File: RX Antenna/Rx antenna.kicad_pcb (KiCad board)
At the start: 2 copper layers, 40 x 40 mm, 11 parts, among them J1 PATCH_FEED, J2 Conn_01x02

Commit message: pcb for rx made
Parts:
- removed D1: MA4E2054A1-287T, Package_TO_SOT_SMD:SOT-23
- removed J2: Conn_01x02, Connector_PinHeader_2.54mm:PinHeader_1x02_P2.54mm_Vertical
- removed JP1: SolderJumper_3_Bridged12, Jumper:SolderJumper-3_P1.3mm_Bridged12_RoundedPad1.0x1.5mm
- removed TP_DC1, TP_RF1, TP_STORE1: TestPoint, TestPoint:TestPoint_Pad_D1.5mm
- added AE1: Antenna, customFootprints:AperturePatch, F.Cu at (115.0, 115.0)
- added C4: 2p, Capacitor_SMD:C_0201_0603Metric_Pad0.64x0.40mm_HandSolder, B.Cu at (128.2, 118.8)
- added C5: 0.1u, Capacitor_SMD:C_0603_1608Metric_Pad1.08x0.95mm_HandSolder, B.Cu at (125.4, 110.0)
- added C6: 10u, Capacitor_SMD:C_0603_1608Metric_Pad1.08x0.95mm_HandSolder, B.Cu at (126.4, 111.1)
- added C7: 0.01u, Capacitor_SMD:C_0603_1608Metric_Pad1.08x0.95mm_HandSolder, B.Cu at (124.5, 117.8)
- added C8: 0.76pF, customFootprints:C_0201_branch, B.Cu at (121.0, 124.1)
- added CR1: SMS7630-006LF, Package_TO_SOT_SMD:SOT-23, B.Cu at (126.0, 119.8)
- added D2: LED, LED_SMD:LED_0603_1608Metric_Pad1.05x0.95mm_HandSolder, B.Cu at (121.8, 105.2)
- added D3: LED, LED_SMD:LED_0603_1608Metric_Pad1.05x0.95mm_HandSolder, B.Cu at (120.7, 106.3)
- added L2: 22u, Inductor_SMD:L_1210_3225Metric_Pad1.42x2.65mm_HandSolder, B.Cu at (128.3, 114.3)
- added Q1: AO3400A, Package_TO_SOT_SMD:SOT-23, B.Cu at (123.5, 108.4)
- added R1: 10M, Resistor_SMD:R_0603_1608Metric_Pad0.98x0.95mm_HandSolder, B.Cu at (121.6, 117.7)
- added R10: 0, Resistor_SMD:R_0603_1608Metric_Pad0.98x0.95mm_HandSolder, B.Cu at (118.0, 107.4)
- added R11: 0, Resistor_SMD:R_0603_1608Metric_Pad0.98x0.95mm_HandSolder, B.Cu at (119.4, 102.8)
- added R12: 0, Resistor_SMD:R_0603_1608Metric_Pad0.98x0.95mm_HandSolder, B.Cu at (118.3, 103.9)
- added R2: 4.42M, Resistor_SMD:R_0603_1608Metric_Pad0.98x0.95mm_HandSolder, B.Cu at (119.3, 120.0)
- added R3: 3.65M, Resistor_SMD:R_0603_1608Metric_Pad0.98x0.95mm_HandSolder, B.Cu at (120.5, 116.6)
- added R4: 4.42M, Resistor_SMD:R_0603_1608Metric_Pad0.98x0.95mm_HandSolder, B.Cu at (118.2, 118.9)
- added R5: 10M, Resistor_SMD:R_0603_1608Metric_Pad0.98x0.95mm_HandSolder, B.Cu at (129.3, 118.5)
- added R6: 10M, Resistor_SMD:R_0603_1608Metric_Pad0.98x0.95mm_HandSolder, B.Cu at (129.3, 121.9)
- added R7: 10M, Resistor_SMD:R_0603_1608Metric_Pad0.98x0.95mm_HandSolder, B.Cu at (119.3, 110.9)
- added R8: 0, Resistor_SMD:R_0603_1608Metric_Pad0.98x0.95mm_HandSolder, B.Cu at (116.9, 108.5)
- added R9: 10M, Resistor_SMD:R_0603_1608Metric_Pad0.98x0.95mm_HandSolder, B.Cu at (120.4, 109.8)
- added U1: BQ25504, Package_DFN_QFN:VQFN-16-1EP_3x3mm_P0.5mm_EP1.68x1.68mm, B.Cu at (123.8, 114.4)
- C1: value 2.2pF -> 0.76pF; footprint Capacitor_SMD:C_0402_1005Metric -> Capacitor_SMD:C_0201_0603Metric_Pad0.64x0.40mm_HandSolder; moved to B.Cu
- C2: value 10nF -> 2p; footprint Capacitor_SMD:C_0402_1005Metric -> Capacitor_SMD:C_0201_0603Metric_Pad0.64x0.40mm_HandSolder; moved to B.Cu
- C3: value 100mF 5.5V -> 3mF
- J1: value PATCH_FEED -> Conn_Coaxial; footprint Connector_PinHeader_2.54mm:PinHeader_1x01_P2.54mm_Vertical -> Connector_Coaxial:U.FL_Hirose_U.FL-R-SMT-1_Vertical; moved to B.Cu
- L1: value 1.8nH -> 2.51nH; moved to B.Cu
- moved J1 79.7 mm to (121.0, 128.0), turned to -90 degrees
- moved L1 73.6 mm to (122.0, 122.5), turned to 45 degrees
- moved C1 72.3 mm to (121.4, 123.7), turned to -45 degrees
- moved C2 68.7 mm to (123.3, 121.2), turned to 45 degrees
- moved C3 50.5 mm to (125.2, 105.6), turned to -45 degrees
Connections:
- C1 pad 1: Net-(D1-A) -> Net-(AE1-A)
- C2 pad 1: Net-(D1-K) -> Net-(C2-Pad1)
- C2 pad 2: GND -> Net-(C2-Pad2)
- C3 pad 1: Net-(D1-K) -> Net-(U1-VBAT)
- L1 pad 1: Net-(JP1-C) -> Net-(AE1-A)
- L1 pad 2: Net-(D1-A) -> Net-(C2-Pad1)
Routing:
- net GND: track 0.00 -> 19.5 mm, vias 0 -> 8
- net Net-(U1-VRDIV): track 0.00 -> 19.5 mm
- net Net-(U1-VBAT): track 0.00 -> 17.8 mm
- net Net-(U1-OK_HYST): track 0.00 -> 9.16 mm
- net Net-(U1-VOC_SAMP): track 0.00 -> 9.12 mm, vias 0 -> 2
- net Net-(U1-VIN_DC): track 0.00 -> 8.87 mm
- net Net-(U1-OK_PROG): track 0.00 -> 8.09 mm
- net Net-(AE1-A): track 0.00 -> 7.49 mm
- net Net-(Q1-G): track 0.00 -> 6.80 mm
- net Net-(U1-VBAT_OV): track 0.00 -> 5.95 mm
- net Net-(U1-VBAT_UV): track 0.00 -> 5.38 mm
- net Net-(U1-VSTOR): track 0.00 -> 3.69 mm
- net Net-(U1-LBST): track 0.00 -> 3.33 mm
- net Net-(D3-K): track 0.00 -> 2.77 mm
- net Net-(J1-In): track 0.07 -> 2.44 mm
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- added copper zone on B.Cu, net GND
- added copper zone on In2.Cu, net GND
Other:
- board size 40 x 40 mm -> 30 x 30 mm
- copper layers 2 -> 4
- rule pad_to_mask_clearance: 0 -> 0.0508

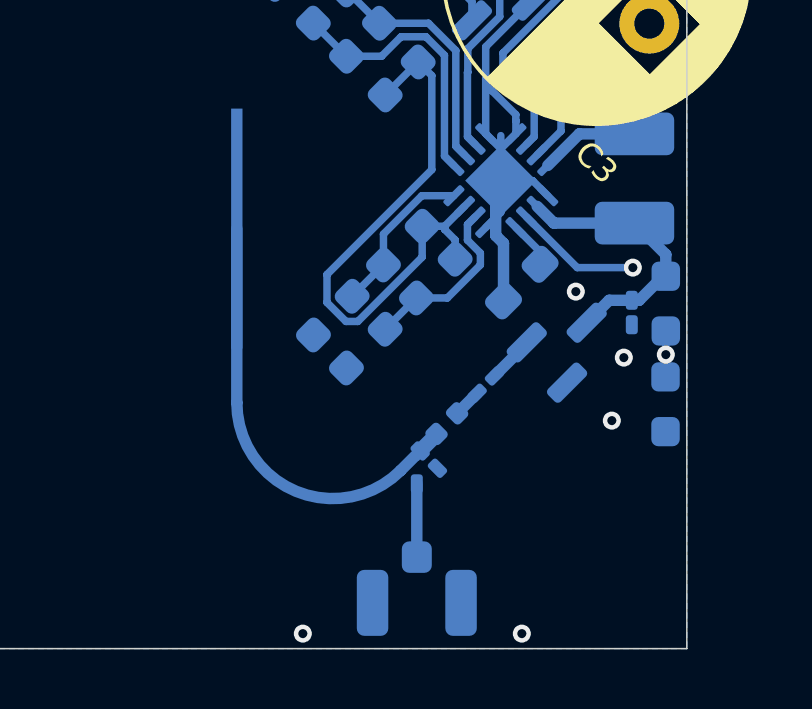
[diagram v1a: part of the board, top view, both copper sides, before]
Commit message: updated impedance matching
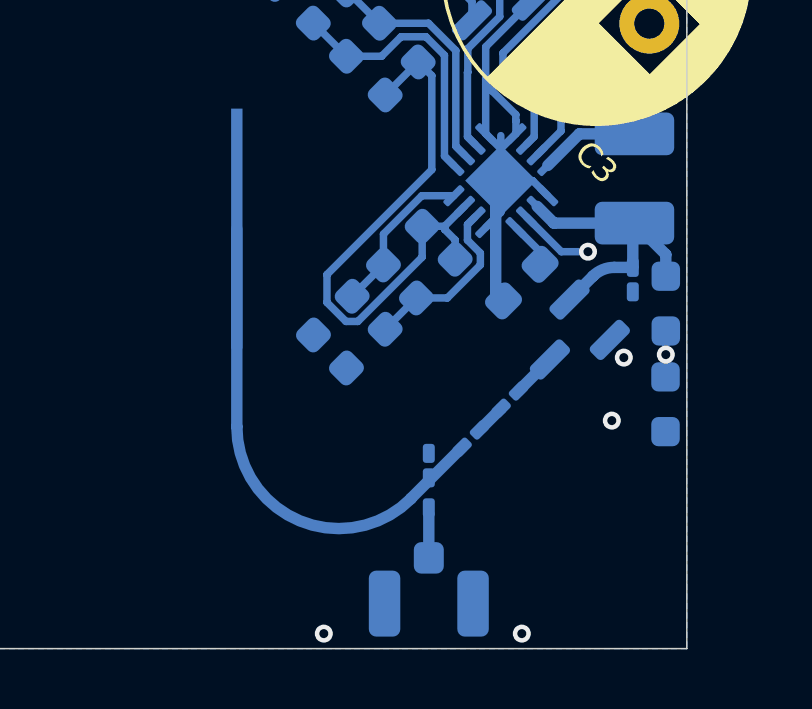
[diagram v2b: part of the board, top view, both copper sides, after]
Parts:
- L1: value 2.51nH -> 2nH; footprint Inductor_SMD:L_0402_1005Metric -> Inductor_SMD:L_0201_0603Metric_Pad0.64x0.40mm_HandSolder
- moved C4 1.10 mm to (128.2, 117.7)
- moved C2 0.94 mm to (124.1, 121.7)
- moved L1 0.94 mm to (122.8, 123.0)
- moved C8 0.89 mm to (121.4, 124.9)
- moved J1 0.64 mm to (121.4, 128.5)
- moved C1 0.20 mm to (121.4, 123.9), turned to 90 degrees
- moved CR1 0.14 mm to (126.1, 119.7), turned to -135 degrees
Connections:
- C4 pad 1: Net-(U1-VIN_DC) -> /RF_VOUT
- CR1 pad 1: GND -> /RF_VOUT
- CR1 pad 2: Net-(C2-Pad2) -> GND
- CR1 pad 3: Net-(U1-VIN_DC) -> Net-(C2-Pad2)
- L2 pad 1: Net-(U1-VIN_DC) -> /RF_VOUT
- R5 pad 1: Net-(U1-VIN_DC) -> /RF_VOUT
- U1 pad 2: Net-(U1-VIN_DC) -> /RF_VOUT
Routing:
- net /RF_VOUT: track 0.00 -> 9.68 mm
- net Net-(U1-VIN_DC): track 8.87 -> 0.00 mm
- net Net-(AE1-A): track 7.49 -> 9.02 mm
- net Net-(J1-In): track 2.44 -> 1.47 mm
- net GND: track 19.5 -> 20.0 mm, vias 8 -> 7

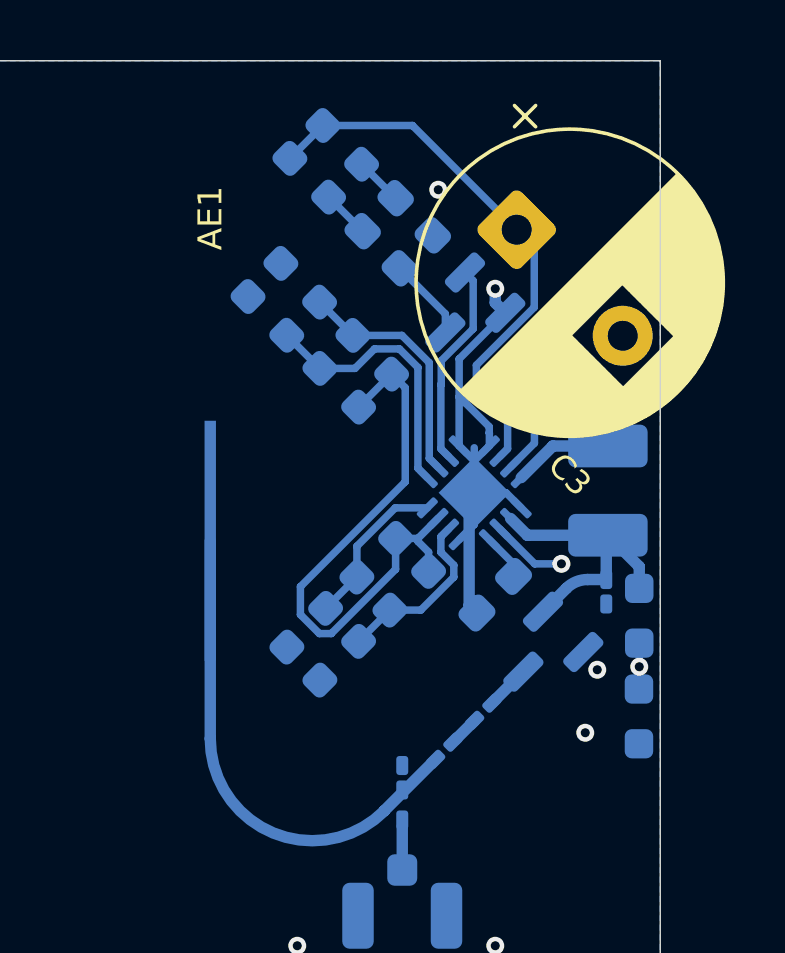
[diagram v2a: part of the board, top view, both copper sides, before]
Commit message: checked drc and fixed gnd plane
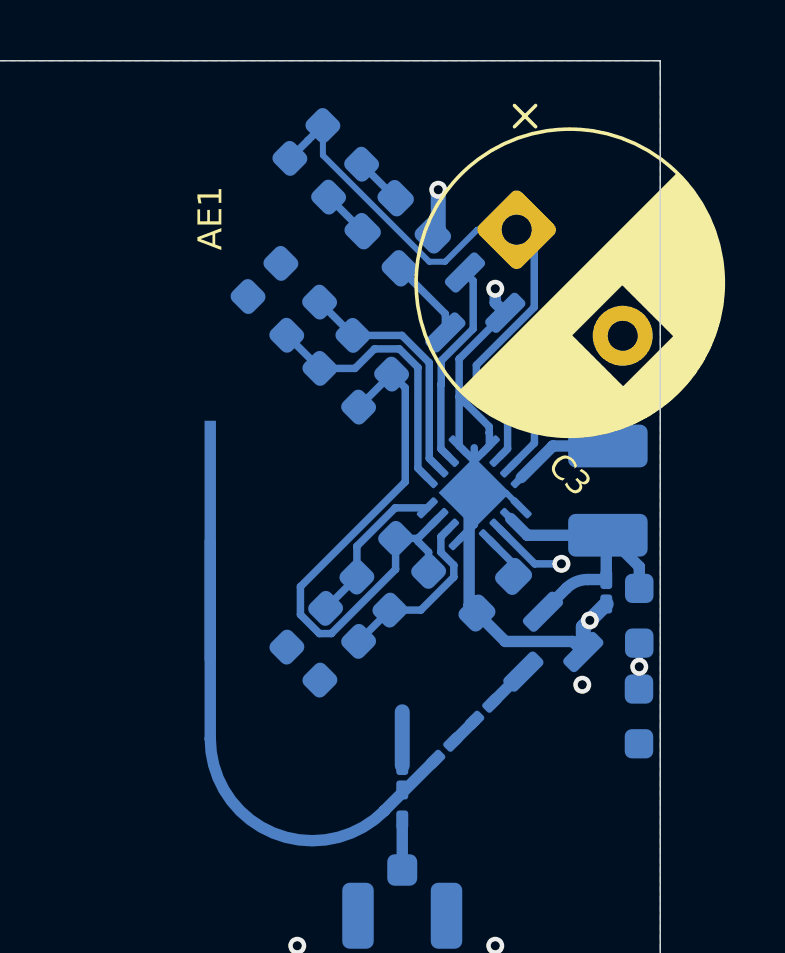
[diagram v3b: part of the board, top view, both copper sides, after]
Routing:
- net GND: track 20.0 -> 29.4 mm, vias 7 -> 6
- net Net-(U1-VBAT): track 17.8 -> 19.2 mm

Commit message: saatvik mad
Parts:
- added C9: 10u, Capacitor_SMD:C_0603_1608Metric_Pad1.08x0.95mm_HandSolder, B.Cu at (129.2, 118.5)
- added JP1: Jumper_2_Open, Jumper:SolderJumper-2_P1.3mm_Open_RoundedPad1.0x1.5mm, B.Cu at (127.5, 107.2)
- C3: value 3mF -> 100mF
- R1: value 10M -> 7.5M
- R2, R4: value 4.42M -> 7.5M
- R3: value 3.65M -> 2.67M
- moved R5 3.30 mm to (129.2, 121.8)
- moved R6 3.30 mm to (129.2, 125.2)
- moved C8 2.23 mm to (123.0, 123.3)
- moved J1 1.77 mm to (123.0, 127.8)
- moved C4 0.70 mm to (127.5, 117.8), turned to -45 degrees
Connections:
- net Net-(U1-VOC_SAMP) renamed /VOC_SAMP
- C8 pad 1: Net-(AE1-A) -> Net-(C2-Pad1)
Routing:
- net /VOC_SAMP: track 9.12 -> 23.5 mm, vias 2 -> 3
- net GND: track 29.4 -> 34.8 mm, vias 6 -> 7
- net Net-(JP1-A): track 3.69 -> 7.63 mm, vias 0 -> 2
- net /RF_VOUT: track 9.68 -> 12.9 mm
- net Net-(J1-In): track 1.47 -> 2.27 mm
